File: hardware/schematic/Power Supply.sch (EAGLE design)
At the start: 15 parts, among them J1 POWER_JACKPTH, U2 RECOM_X.X_REG78XX

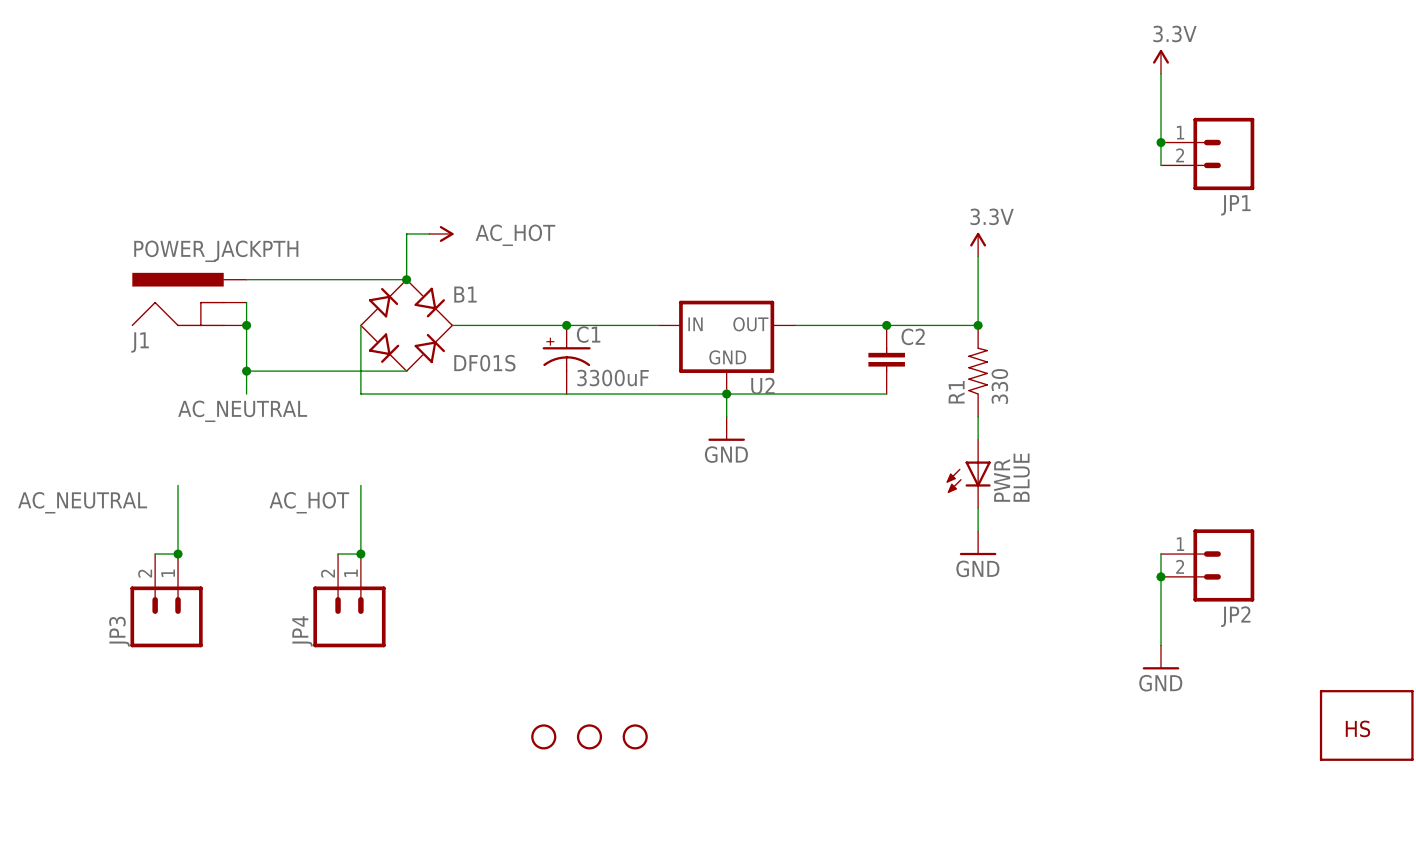
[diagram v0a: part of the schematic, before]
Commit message: Increase trace widths on Power board.  Start motherboard layout
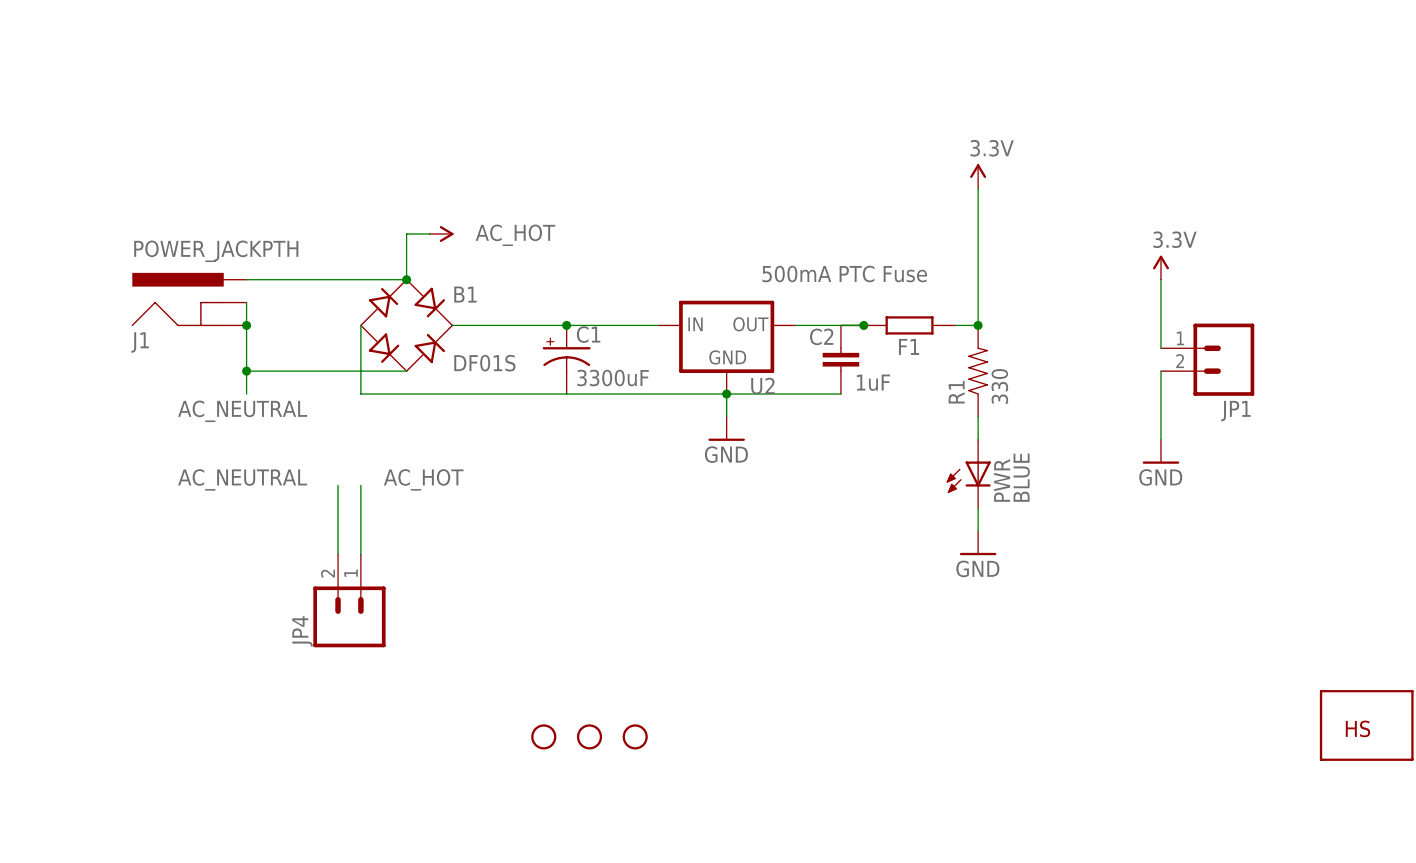
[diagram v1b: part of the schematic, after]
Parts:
- removed JP2, JP3: (no value), SparkFun-Connectors:M02LOCK_LONGPADS
- added F1: 500mA PTC Fuse, resistor:R-EU_M1206
- C2: value (none) -> 1uF
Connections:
- new net N$1: C2.1, F1.2, U2.OUT
- net 3.3V: now also F1.1; no longer C2.1, JP1.2, U2.OUT
- net AC_HOT: no longer JP4.2
- net AC_NEUTRAL: now also JP4.2; no longer JP3.1, JP3.2
- net GND: now also JP1.2; no longer JP2.1, JP2.2
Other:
- moved on the sheet: C2, JP1
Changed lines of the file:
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@@
 <part name="U$2" library="lizardworx" deviceset="VNEG" device="" value="AC_HOT"/>
 <part name="JP1" library="SparkFun-Connectors" deviceset="M02" device="LOCK_LONGPADS"/>
-<part name="JP2" library="SparkFun-Connectors" deviceset="M02" device="LOCK_LONGPADS"/>
-<part name="JP3" library="SparkFun-Connectors" deviceset="M02" device="LOCK_LONGPADS"/>
 <part name="JP4" library="SparkFun-Connectors" deviceset="M02" device="LOCK_LONGPADS"/>
 <part name="P+1" library="SparkFun02-20-08" deviceset="3.3V" device=""/>
-<part name="GND1" library="SparkFun02-20-08" deviceset="GND" device=""/>
 <part name="JP6" library="SparkFun-Electromechanical" deviceset="STAND-OFF" device=""/>
 <part name="JP5" library="SparkFun-Electromechanical" deviceset="STAND-OFF" device=""/>
 <part name="JP8" library="SparkFun-Electromechanical" deviceset="STAND-OFF" device=""/>
 <part name="U$1" library="lizardworx" deviceset="LOGO" device="NORMAL"/>
-<part name="C2" library="SparkFun-Passives" deviceset="CAP" device="0603-CAP"/>
+<part name="C2" library="SparkFun-Passives" deviceset="CAP" device="0603-CAP" value="1uF"/>
+<part name="F1" library="resistor" deviceset="R-EU_" device="M1206" value="500mA PTC Fuse"/>
+<part name="GND1" library="SparkFun02-20-08" deviceset="GND" device=""/>
 </parts>
 <sheets>
@@
 <instance part="C1" gate="G$1" x="190.5" y="144.78"/>
 <instance part="GND3" gate="1" x="208.28" y="134.62"/>
-<instance part="P+18" gate="G$1" x="236.22" y="154.94"/>
+<instance part="P+18" gate="G$1" x="236.22" y="162.56"/>
 <instance part="PWR" gate="G$1" x="236.22" y="132.08"/>
 <instance part="GND4" gate="1" x="236.22" y="121.92"/>
@@
 <attribute name="VALUE" x="189.23" y="158.496" size="1.778" layer="96" rot="R180"/>
 </instance>
-<instance part="JP1" gate="G$1" x="264.16" y="167.64" rot="R180"/>
-<instance part="JP2" gate="G$1" x="264.16" y="121.92" rot="R180"/>
-<instance part="JP3" gate="G$1" x="147.32" y="114.3" rot="R90"/>
+<instance part="JP1" gate="G$1" x="264.16" y="144.78" rot="R180"/>
 <instance part="JP4" gate="G$1" x="167.64" y="114.3" rot="R90"/>
-<instance part="P+1" gate="G$1" x="256.54" y="175.26"/>
-<instance part="GND1" gate="1" x="256.54" y="109.22"/>
+<instance part="P+1" gate="G$1" x="256.54" y="152.4"/>
 <instance part="JP6" gate="G$1" x="187.96" y="101.6"/>
 <instance part="JP5" gate="G$1" x="193.04" y="101.6"/>
 <instance part="JP8" gate="G$1" x="198.12" y="101.6"/>
 <instance part="U$1" gate="G$1" x="276.86" y="101.6"/>
-<instance part="C2" gate="G$1" x="226.06" y="142.24"/>
+<instance part="C2" gate="G$1" x="220.98" y="142.24" smashed="yes">
+<attribute name="NAME" x="217.424" y="145.161" size="1.778" layer="95"/>
+<attribute name="VALUE" x="222.504" y="140.081" size="1.778" layer="96"/>
+</instance>
+<instance part="F1" gate="G$1" x="228.6" y="147.32" smashed="yes" rot="R180">
+<attribute name="NAME" x="229.87" y="145.8214" size="1.778" layer="95" rot="R180"/>
+<attribute name="VALUE" x="212.09" y="152.146" size="1.778" layer="96"/>
+</instance>
+<instance part="GND1" gate="1" x="256.54" y="132.08"/>
 </instances>
 <busses>
@@
 <wire x1="167.64" y1="139.7" x2="190.5" y2="139.7" width="0.1524" layer="91"/>
 <pinref part="U2" gate="G$1" pin="GND"/>
-<wire x1="226.06" y1="139.7" x2="208.28" y2="139.7" width="0.1524" layer="91"/>
+<wire x1="220.98" y1="139.7" x2="208.28" y2="139.7" width="0.1524" layer="91"/>
 <wire x1="208.28" y1="139.7" x2="190.5" y2="139.7" width="0.1524" layer="91"/>
 <junction x="208.28" y="139.7"/>
@@
 </segment>
 <segment>
-<pinref part="JP2" gate="G$1" pin="1"/>
-<pinref part="JP2" gate="G$1" pin="2"/>
-<wire x1="256.54" y1="121.92" x2="256.54" y2="119.38" width="0.1524" layer="91"/>
-<wire x1="256.54" y1="119.38" x2="256.54" y2="111.76" width="0.1524" layer="91"/>
-<junction x="256.54" y="119.38"/>
+<pinref part="JP1" gate="G$1" pin="2"/>
 <pinref part="GND1" gate="1" pin="GND"/>
+<wire x1="256.54" y1="134.62" x2="256.54" y2="142.24" width="0.1524" layer="91"/>
 </segment>
 </net>
 <net name="3.3V" class="0">
 <segment>
-<pinref part="U2" gate="G$1" pin="OUT"/>
-<wire x1="215.9" y1="147.32" x2="226.06" y2="147.32" width="0.1524" layer="91"/>
-<wire x1="226.06" y1="147.32" x2="236.22" y2="147.32" width="0.1524" layer="91"/>
-<wire x1="236.22" y1="147.32" x2="236.22" y2="154.94" width="0.1524" layer="91"/>
-<pinref part="P+18" gate="G$1" pin="3.3V"/>
-<pinref part="R1" gate="G$1" pin="2"/>
-<junction x="236.22" y="147.32"/>
-<pinref part="C2" gate="G$1" pin="1"/>
-<junction x="226.06" y="147.32"/>
+<pinref part="JP1" gate="G$1" pin="1"/>
+<wire x1="256.54" y1="144.78" x2="256.54" y2="152.4" width="0.1524" layer="91"/>
+<pinref part="P+1" gate="G$1" pin="3.3V"/>
 </segment>
 <segment>
-<pinref part="JP1" gate="G$1" pin="2"/>
-<pinref part="JP1" gate="G$1" pin="1"/>
-<wire x1="256.54" y1="165.1" x2="256.54" y2="167.64" width="0.1524" layer="91"/>
-<wire x1="256.54" y1="167.64" x2="256.54" y2="175.26" width="0.1524" layer="91"/>
-<junction x="256.54" y="167.64"/>
-<pinref part="P+1" gate="G$1" pin="3.3V"/>
+<pinref part="R1" gate="G$1" pin="2"/>
+<pinref part="F1" gate="G$1" pin="1"/>
+<wire x1="233.68" y1="147.32" x2="236.22" y2="147.32" width="0.1524" layer="91"/>
+<pinref part="P+18" gate="G$1" pin="3.3V"/>
+<wire x1="236.22" y1="147.32" x2="236.22" y2="162.56" width="0.1524" layer="91"/>
+<junction x="236.22" y="147.32"/>
 </segment>
 </net>
@@
 </segment>
 <segment>
-<pinref part="JP3" gate="G$1" pin="2"/>
-<pinref part="JP3" gate="G$1" pin="1"/>
-<wire x1="144.78" y1="121.92" x2="147.32" y2="121.92" width="0.1524" layer="91"/>
-<wire x1="147.32" y1="121.92" x2="147.32" y2="129.54" width="0.1524" layer="91"/>
-<junction x="147.32" y="121.92"/>
-<label x="129.54" y="127" size="1.778" layer="95"/>
+<pinref part="JP4" gate="G$1" pin="2"/>
+<wire x1="165.1" y1="121.92" x2="165.1" y2="129.54" width="0.1524" layer="91"/>
+<label x="147.32" y="129.54" size="1.778" layer="95"/>
 </segment>
 </net>
@@
 </segment>
 <segment>
-<pinref part="JP4" gate="G$1" pin="2"/>
 <pinref part="JP4" gate="G$1" pin="1"/>
-<wire x1="165.1" y1="121.92" x2="167.64" y2="121.92" width="0.1524" layer="91"/>
 <wire x1="167.64" y1="121.92" x2="167.64" y2="129.54" width="0.1524" layer="91"/>
-<junction x="167.64" y="121.92"/>
-<label x="157.48" y="127" size="1.778" layer="95"/>
+<label x="170.18" y="129.54" size="1.778" layer="95"/>
 </segment>
 </net>
+<net name="N$1" class="0">
+<segment>
+<pinref part="C2" gate="G$1" pin="1"/>
+<pinref part="U2" gate="G$1" pin="OUT"/>
+<wire x1="215.9" y1="147.32" x2="223.52" y2="147.32" width="0.1524" layer="91"/>
+<pinref part="F1" gate="G$1" pin="2"/>
+<junction x="223.52" y="147.32"/>
+<wire x1="223.52" y1="147.32" x2="220.98" y2="147.32" width="0.1524" layer="91"/>
+</segment>
+</net>
